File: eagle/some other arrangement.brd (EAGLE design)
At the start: 22 parts

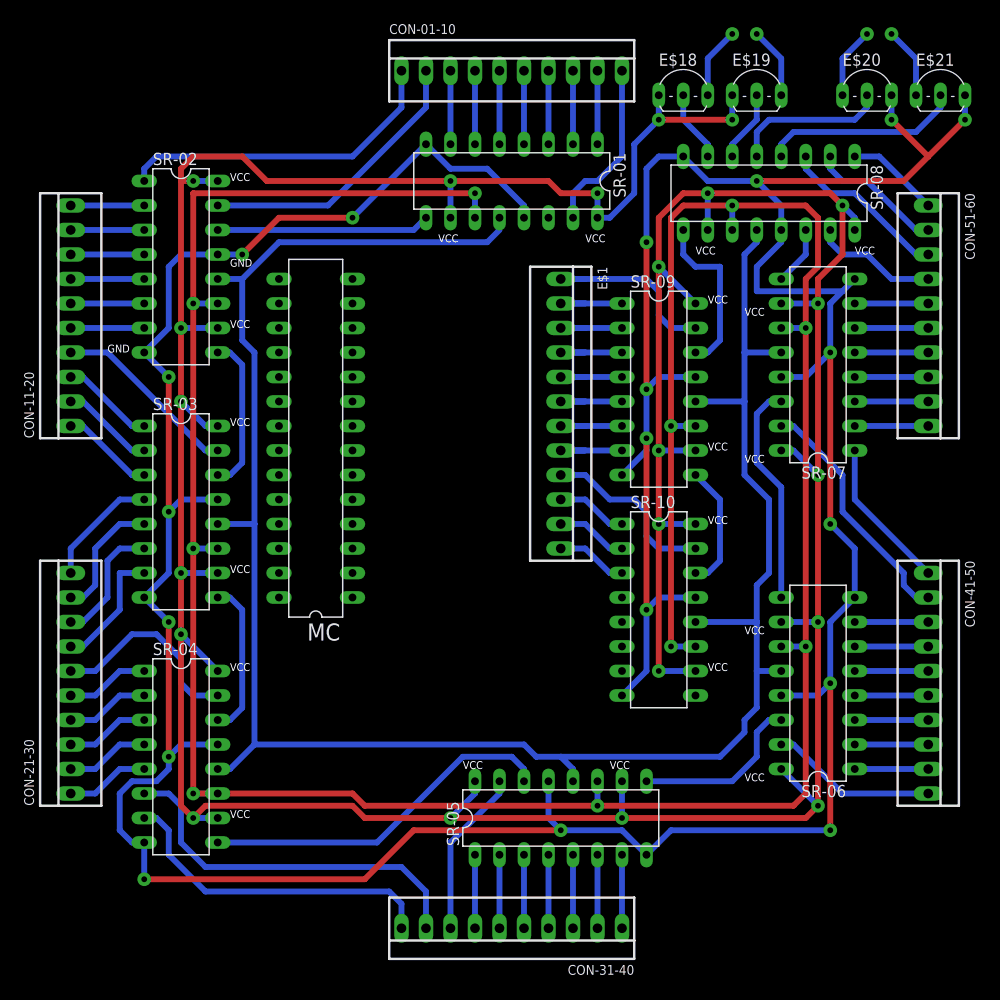
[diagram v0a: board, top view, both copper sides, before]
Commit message: conectat pini shift registers cu toate oputputurile
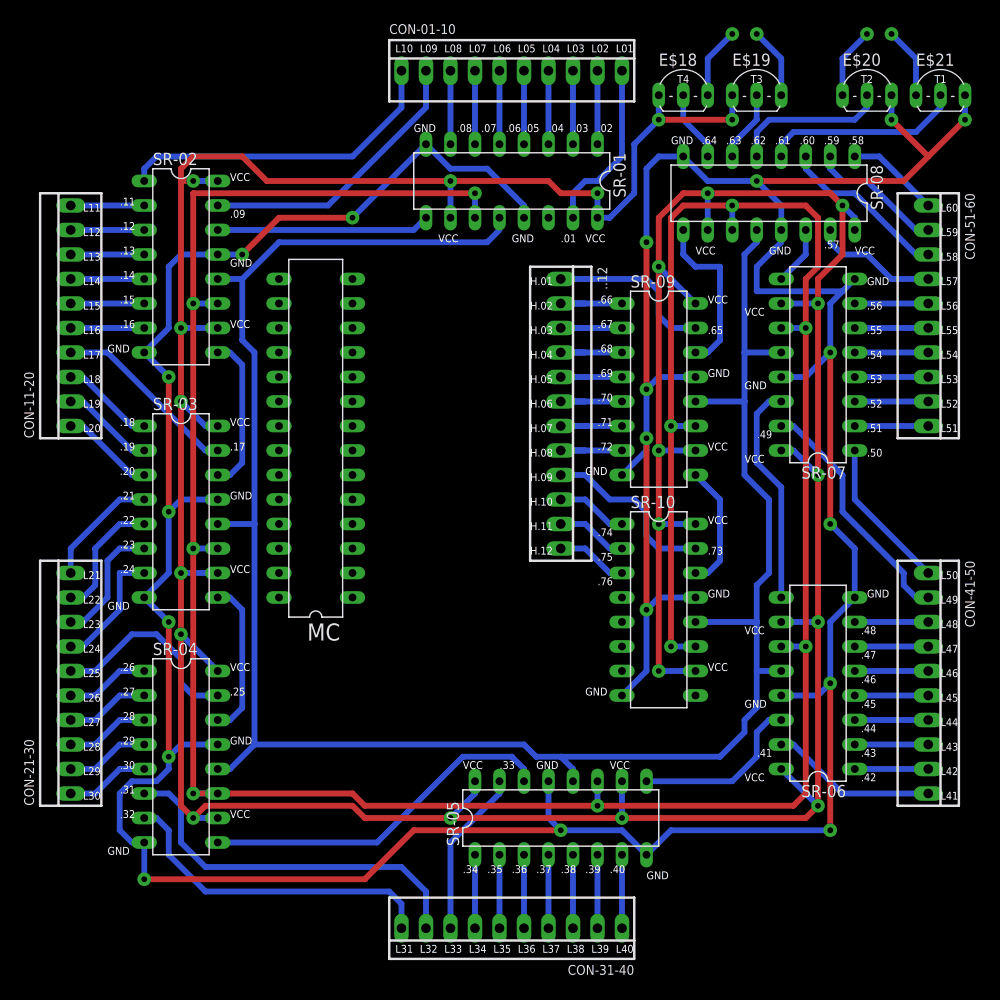
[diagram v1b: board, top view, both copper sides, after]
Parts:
- renumbered E$1 to ..12
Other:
- board text added: ".01"
- board text added: ".02"
- board text added: ".03"
- board text added: ".04"
- board text added: ".05"
- board text added: ".06"
- board text added: ".07"
- board text added: ".08"
- board text added: ".09"
- board text added: ".11"
- board text added: ".12"
- board text added: ".13"
- board text added: ".14"
- board text added: ".15"
- board text added: ".16"
- board text added: ".17"
- board text added: ".18"
- board text added: ".19"
- board text added: ".20"
- board text added: ".21"
- board text added: ".22"
- board text added: ".23"
- board text added: ".24"
- board text added: ".25"
- board text added: ".26"
- board text added: ".27"
- board text added: ".28"
- board text added: ".29"
- board text added: ".30"
- board text added: ".31"
- board text added: ".32"
- board text added: ".33"
- board text added: ".34"
- board text added: ".35"
- board text added: ".36"
- board text added: ".37"
- board text added: ".38"
- board text added: ".39"
- board text added: ".40"
- board text added: ".41"
- board text added: ".42"
- board text added: ".43"
- board text added: ".44"
- board text added: ".45"
- board text added: ".46"
- board text added: ".47"
- board text added: ".48"
- board text added: ".49"
- board text added: ".50"
- board text added: ".51"
- board text added: ".52"
- board text added: ".53"
- board text added: ".54"
- board text added: ".55"
- board text added: ".56"
- board text added: ".57"
- board text added: ".58"
- board text added: ".59"
- board text added: ".60"
- board text added: ".61"
- board text added: ".62"
- board text added: ".63"
- board text added: ".64"
- board text added: ".65"
- board text added: ".66"
- board text added: ".67"
- board text added: ".68"
- board text added: ".69"
- board text added: ".70"
- board text added: ".71"
- board text added: ".72"
- board text added: ".73"
- board text added: ".74"
- board text added: ".75"
- board text added: ".76"
- board text added: "H.01"
- board text added: "H.02"
- board text added: "H.03"
- board text added: "H.04"
- board text added: "H.05"
- board text added: "H.06"
- board text added: "H.07"
- board text added: "H.08"
- board text added: "H.09"
- board text added: "H.10"
- board text added: "H.11"
- board text added: "H.12"
- board text added: "L01"
- board text added: "L02"
- board text added: "L03"
- board text added: "L04"
- board text added: "L05"
- board text added: "L06"
- board text added: "L07"
- board text added: "L08"
- board text added: "L09"
- board text added: "L10"
- board text added: "L11"
- board text added: "L12"
- board text added: "L13"
- board text added: "L14"
- board text added: "L15"
- board text added: "L16"
- board text added: "L17"
- board text added: "L18"
- board text added: "L19"
- board text added: "L20"
- board text added: "L21"
- board text added: "L22"
- board text added: "L23"
- board text added: "L24"
- board text added: "L25"
- board text added: "L26"
- board text added: "L27"
- board text added: "L28"
- board text added: "L29"
- board text added: "L30"
- board text added: "L31"
- board text added: "L32"
- board text added: "L33"
- board text added: "L34"
- board text added: "L35"
- board text added: "L36"
- board text added: "L37"
- board text added: "L38"
- board text added: "L39"
- board text added: "L40"
- board text added: "L41"
- board text added: "L42"
- board text added: "L43"
- board text added: "L44"
- board text added: "L45"
- board text added: "L46"
- board text added: "L47"
- board text added: "L48"
- board text added: "L49"
- board text added: "L50"
- board text added: "L51"
- board text added: "L52"
- board text added: "L53"
- board text added: "L54"
- board text added: "L55"
- board text added: "L56"
- board text added: "L57"
- board text added: "L58"
- board text added: "L59"
- board text added: "L60"
- board text added: "T1"
- board text added: "T2"
- board text added: "T3"
- board text added: "T4"

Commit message: 8 pini de proba pentru circuitul RTC
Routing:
- net S$95: vias 1 -> 9
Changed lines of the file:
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@@
 <wire x1="71.12" y1="91.44" x2="71.12" y2="95.25" width="0.6096" layer="16"/>
 <wire x1="71.12" y1="95.25" x2="73.66" y2="97.79" width="0.6096" layer="16"/>
+<via x="55.88" y="27.94" extent="1-16" drill="0.6" diameter="1.4224"/>
+<via x="53.34" y="27.94" extent="1-16" drill="0.6" diameter="1.4224"/>
+<via x="50.8" y="27.94" extent="1-16" drill="0.6" diameter="1.4224"/>
+<via x="48.26" y="27.94" extent="1-16" drill="0.6" diameter="1.4224"/>
+<via x="45.72" y="27.94" extent="1-16" drill="0.6" diameter="1.4224"/>
+<via x="43.18" y="27.94" extent="1-16" drill="0.6" diameter="1.4224"/>
+<via x="40.64" y="27.94" extent="1-16" drill="0.6" diameter="1.4224"/>
+<via x="38.1" y="27.94" extent="1-16" drill="0.6" diameter="1.4224"/>
 </signal>
 <signal name="S$96">

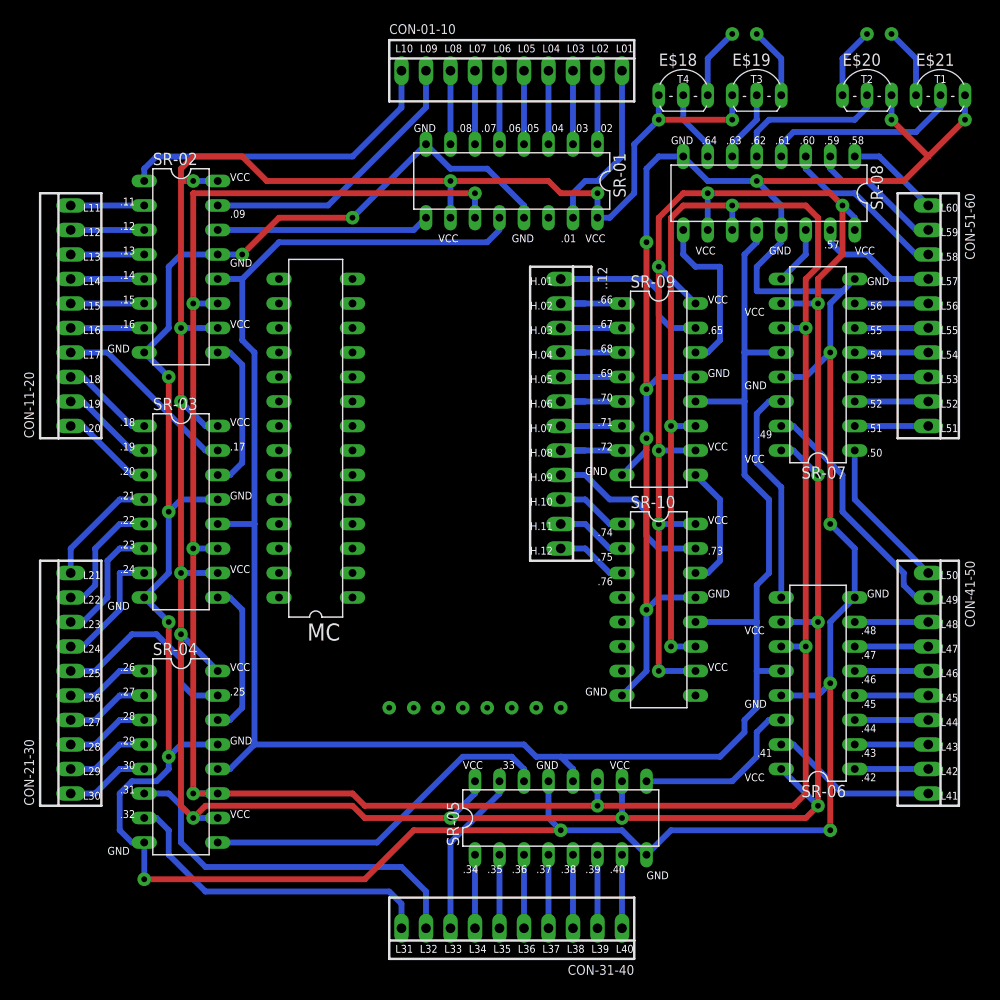
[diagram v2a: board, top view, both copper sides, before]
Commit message: Verificare amanuntita a conexiunilor de pana acum
Raman de verificat GND celelalte 2 semnale de date de la shift register
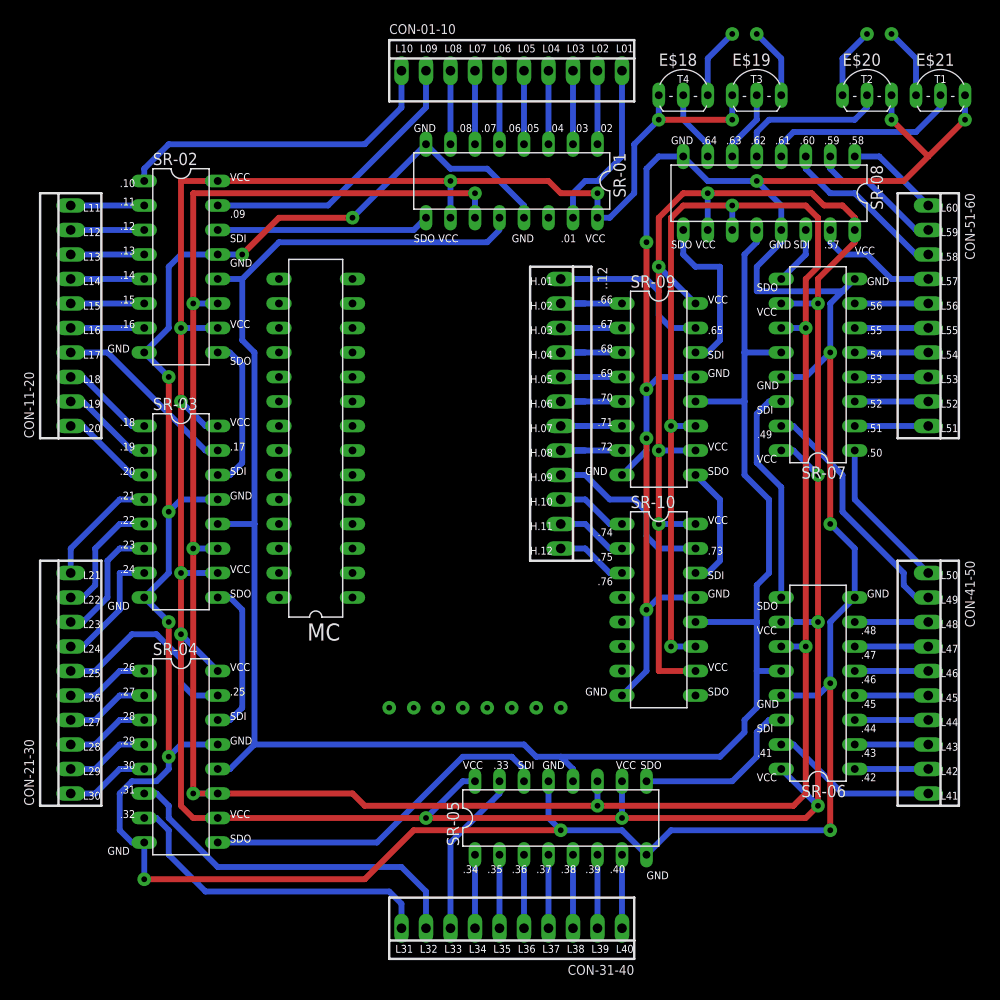
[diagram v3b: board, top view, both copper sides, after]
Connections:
- net S$49: no longer SR-04.10, SR-08.16
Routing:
- net S$49: track 417.4 -> 406.9 mm, vias 22 -> 18
- net S$31: track 39.5 -> 38.0 mm
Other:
- board text added: ".10"
- board text added: "SDI"
- board text added: "SDO"

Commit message: Completat CHECKPOINT 1
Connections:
- new net S$101: SR-02.13
- new net S$91: SR-01.13, SR-01.8
- net S$102: now also E$20.B, E$21.B, SR-03.8, SR-04.13, SR-04.8, SR-05.13, SR-05.8, SR-06.13, SR-06.8, SR-07.13, SR-07.8, SR-08.13, SR-08.8, SR-09.13, SR-09.8
- net S$93: no longer E$20.B, E$21.B, SR-01.13, SR-01.8, SR-02.13, SR-03.8, SR-04.13, SR-04.8, SR-05.13, SR-05.8, SR-06.13, SR-06.8, SR-07.13, SR-07.8, SR-08.13, SR-08.8, SR-09.13, SR-09.8
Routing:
- net S$93: track 391.8 -> 33.0 mm, vias 17 -> 2
- net S$102: track 33.3 -> 341.5 mm, vias 2 -> 11
- net S$91: track 0.00 -> 42.3 mm, vias 0 -> 1
- net S$101: track 0.00 -> 5.08 mm
- net S$80: track 216.7 -> 218.7 mm
- net S$81: vias 10 -> 9
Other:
- board text added: "RCL"
- board text added: "SRC"
